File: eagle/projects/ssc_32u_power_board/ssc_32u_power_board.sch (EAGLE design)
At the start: 36 parts, among them J1 691256610002, J10 ESQ-104-24-H-S, J11 ESQ-104-24-H-S, J12 ESQ-104-24-H-S, J13 ESQ-104-24-H-S, J14 MOL-SL-3-RA, J15 ESQ-103-24-H-S, J16 691256610002, J17 HMTSW-104-08-G-S-380, J18 HMTSW-104-08-G-S-380, J19 HMTSW-104-08-G-S-380, J2 HMTSW-104-08-G-S-380, J20 HMTSW-104-08-G-S-380, J21 ESQ-104-24-H-S, J22 ESQ-104-24-H-S, J23 ESQ-104-24-H-S, J24 ESQ-104-24-H-S, J25 ESQ-104-24-H-S, J26 ESQ-104-24-H-S, J27 ESQ-104-24-H-S, J28 ESQ-104-24-H-S, J3 HMTSW-104-08-G-S-380, J4 HMTSW-104-08-G-S-380, J5 HMTSW-104-08-G-S-380, J6 ESQ-104-24-H-S, J7 ESQ-104-24-H-S, J8 ESQ-104-24-H-S, J9 ESQ-104-24-H-S

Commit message: Finished board layout, used polygons to fill all high current traces
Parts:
- removed J10, J11, J12, J13, J21, J22, J23, J24, J25, J26, J27, J28: ESQ-104-24-H-S, ssc_32u_power_board:ESQ-104-24-H-S
- removed J17, J18, J19, J20: HMTSW-104-08-G-S-380, ssc_32u_power_board:HMTSW-104-08-G-S-380
- added F5, F6, F7, F8: 8A, 35V, ssc_32u_power_board:0437008.WR
- F1, F2, F3, F4: value 0751.0507 -> 8A, 35V; device ssc_32u_power_board:0751.0507 -> ssc_32u_power_board:0437008.WR
- J2, J3, J4, J5: value HMTSW-104-08-G-S-380 -> 4x3_2.54MM_HEADER; device ssc_32u_power_board:HMTSW-104-08-G-S-380 -> ssc_32u_power_board:2X_ESQ-104-24-H-S__HMTSW-104-08-G-S-380
- J6, J7, J8, J9: value ESQ-104-24-H-S -> 4x3_2.54MM_HEADER; device ssc_32u_power_board:ESQ-104-24-H-S -> ssc_32u_power_board:2X_ESQ-104-24-H-S__HMTSW-104-08-G-S-380
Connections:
- removed net BATT_1_FUSE_0_7: F1.P$2, S1.P$1
- removed net BATT_1_FUSE_8_15: F2.P$2, S2.P$1
- removed net BATT_1_SWITCH_0_7: J2.P$1, J2.P$2, J2.P$3, J2.P$4, J3.P$1, J3.P$2, J3.P$3, J3.P$4, S1.P$2
- removed net BATT_1_SWITCH_8_15: J4.P$1, J4.P$2, J4.P$3, J4.P$4, J5.P$1, J5.P$2, J5.P$3, J5.P$4, S2.P$2
- removed net BATT_2_FUSE_16_23: F3.P$2, S3.P$1
- removed net BATT_2_FUSE_24_31: F4.P$2, S4.P$1
- removed net BATT_2_SWITCH_16_23: J17.P$1, J17.P$2, J17.P$3, J17.P$4, J18.P$1, J18.P$2, J18.P$3, J18.P$4, S3.P$2
- removed net BATT_2_SWITCH_24_31: J19.P$1, J19.P$2, J19.P$3, J19.P$4, J20.P$1, J20.P$2, J20.P$3, J20.P$4, S4.P$2
- new net VBAT_1_FUSE_0_3: F1.P$2, J2.V1, J2.V2, J2.V3, J2.V4
- new net VBAT_1_FUSE_12_15: F4.P$2, J5.V1, J5.V2, J5.V3, J5.V4
- new net VBAT_1_FUSE_4_7: F2.P$2, J3.V1, J3.V2, J3.V3, J3.V4
- new net VBAT_1_FUSE_8_11: F3.P$2, J4.V1, J4.V2, J4.V3, J4.V4
- new net VBAT_1_SWITCH_0_7: F1.P$1, F2.P$1, S1.P$2
- new net VBAT_1_SWITCH_8_15: F3.P$1, F4.P$1, S2.P$2
- new net VBAT_2_FUSE_16_19: F5.P$2, J6.V1, J6.V2, J6.V3, J6.V4
- new net VBAT_2_FUSE_20_23: F6.P$2, J7.V1, J7.V2, J7.V3, J7.V4
- new net VBAT_2_FUSE_24_27: F7.P$2, J8.V1, J8.V2, J8.V3, J8.V4
- new net VBAT_2_FUSE_28_31: F8.P$2, J9.V1, J9.V2, J9.V3, J9.V4
- new net VBAT_2_SWITCH_16_23: F5.P$1, F6.P$1, S3.P$2
- new net VBAT_2_SWITCH_24_31: F7.P$1, F8.P$1, S4.P$2
- net BATT_1_VDD: now also S1.P$1, S2.P$1; no longer F1.P$1, F2.P$1
- net BATT_2_VDD: now also J16.BAT_VDD, S3.P$1, S4.P$1; no longer F3.P$1, F4.P$1, J16.BAT_GND
- net GND: now also J16.BAT_GND, J2.G1, J2.G2, J2.G3, J2.G4, J3.G1, J3.G2, J3.G3, J3.G4, J4.G1, J4.G2, J4.G3, J4.G4, J5.G1, J5.G2, J5.G3, J5.G4, J6.G1, J6.G2, J6.G3, J6.G4, J7.G1, J7.G2, J7.G3, J7.G4, J8.G1, J8.G2, J8.G3, J8.G4, J9.G1, J9.G2, J9.G3, J9.G4; no longer J10.P$1, J10.P$2, J10.P$3, J10.P$4, J11.P$1, J11.P$2, J11.P$3, J11.P$4, J12.P$1, J12.P$2, J12.P$3, J12.P$4, J13.P$1, J13.P$2, J13.P$3, J13.P$4, J16.BAT_VDD, J25.P$1, J25.P$2, J25.P$3, J25.P$4, J26.P$1, J26.P$2, J26.P$3, J26.P$4, J27.P$1, J27.P$2, J27.P$3, J27.P$4, J28.P$1, J28.P$2, J28.P$3, J28.P$4
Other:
- note removed: "4PPIN GND HEADER - PINS 0-15"
- note removed: "4PPIN GND HEADER - PINS 16-31"
- note removed: "4PPIN PWM HEADER - PINS 0-15"
- note removed: "4PPIN PWM HEADER - PINS 16-31"

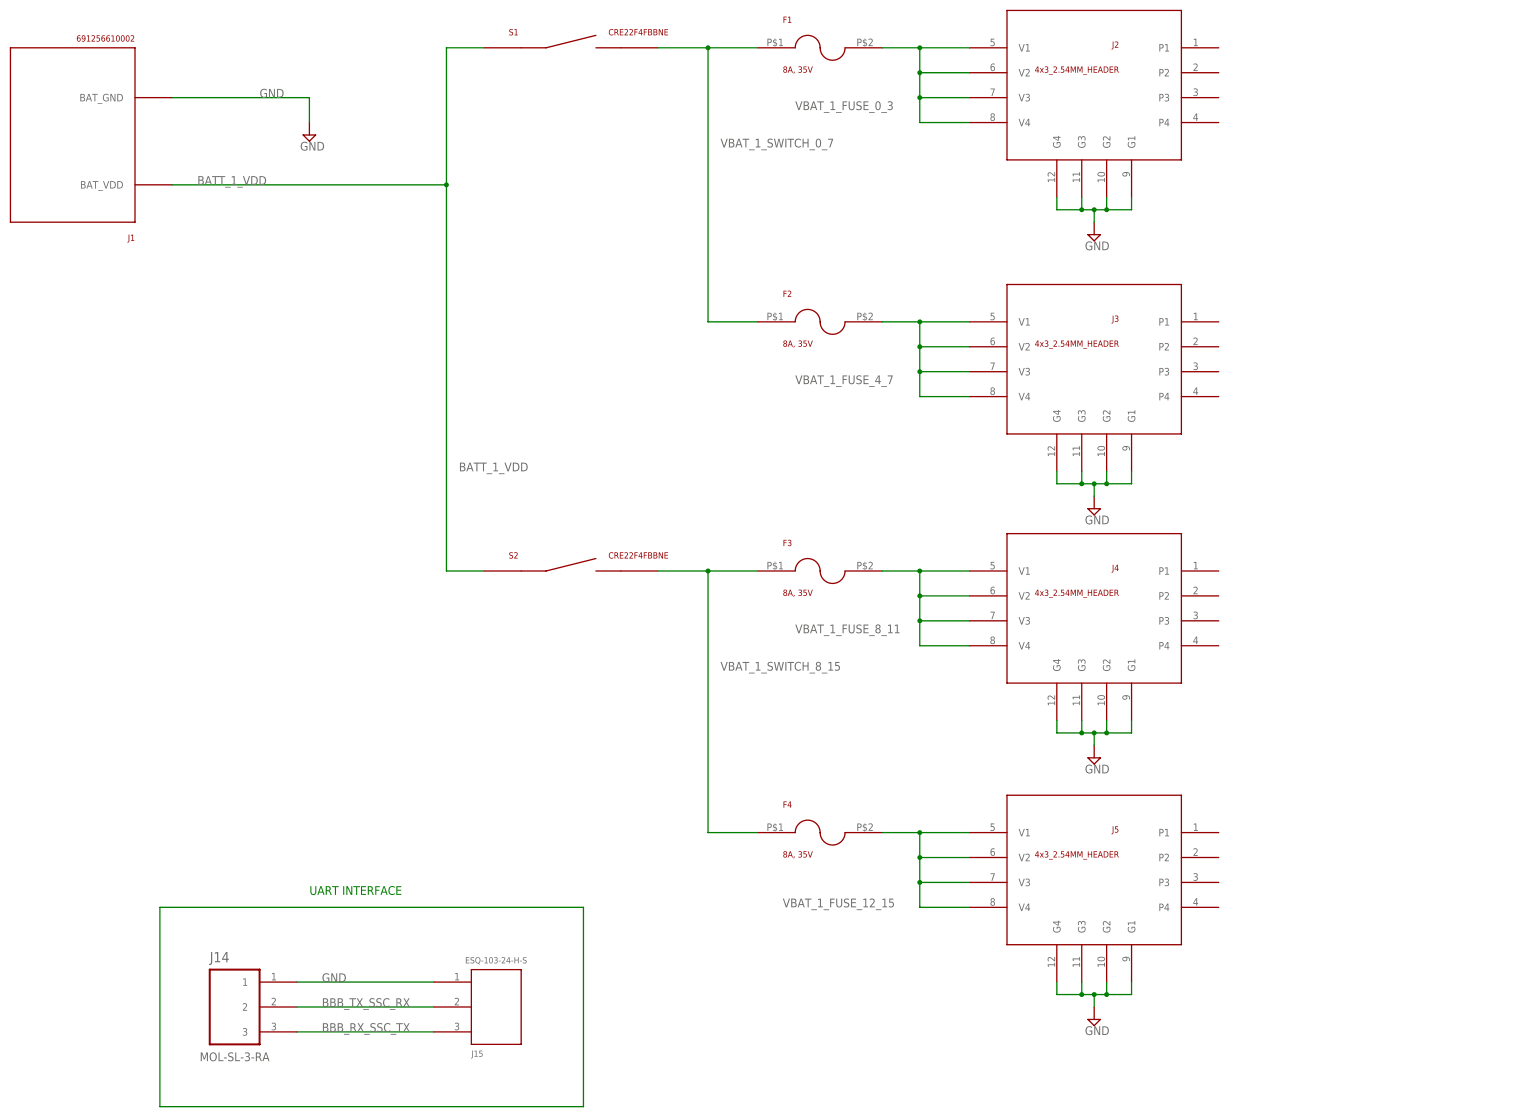
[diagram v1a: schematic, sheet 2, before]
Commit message: Major modifications, removed switches and swapped out surface mount fuses for glass ones. Still two layer board
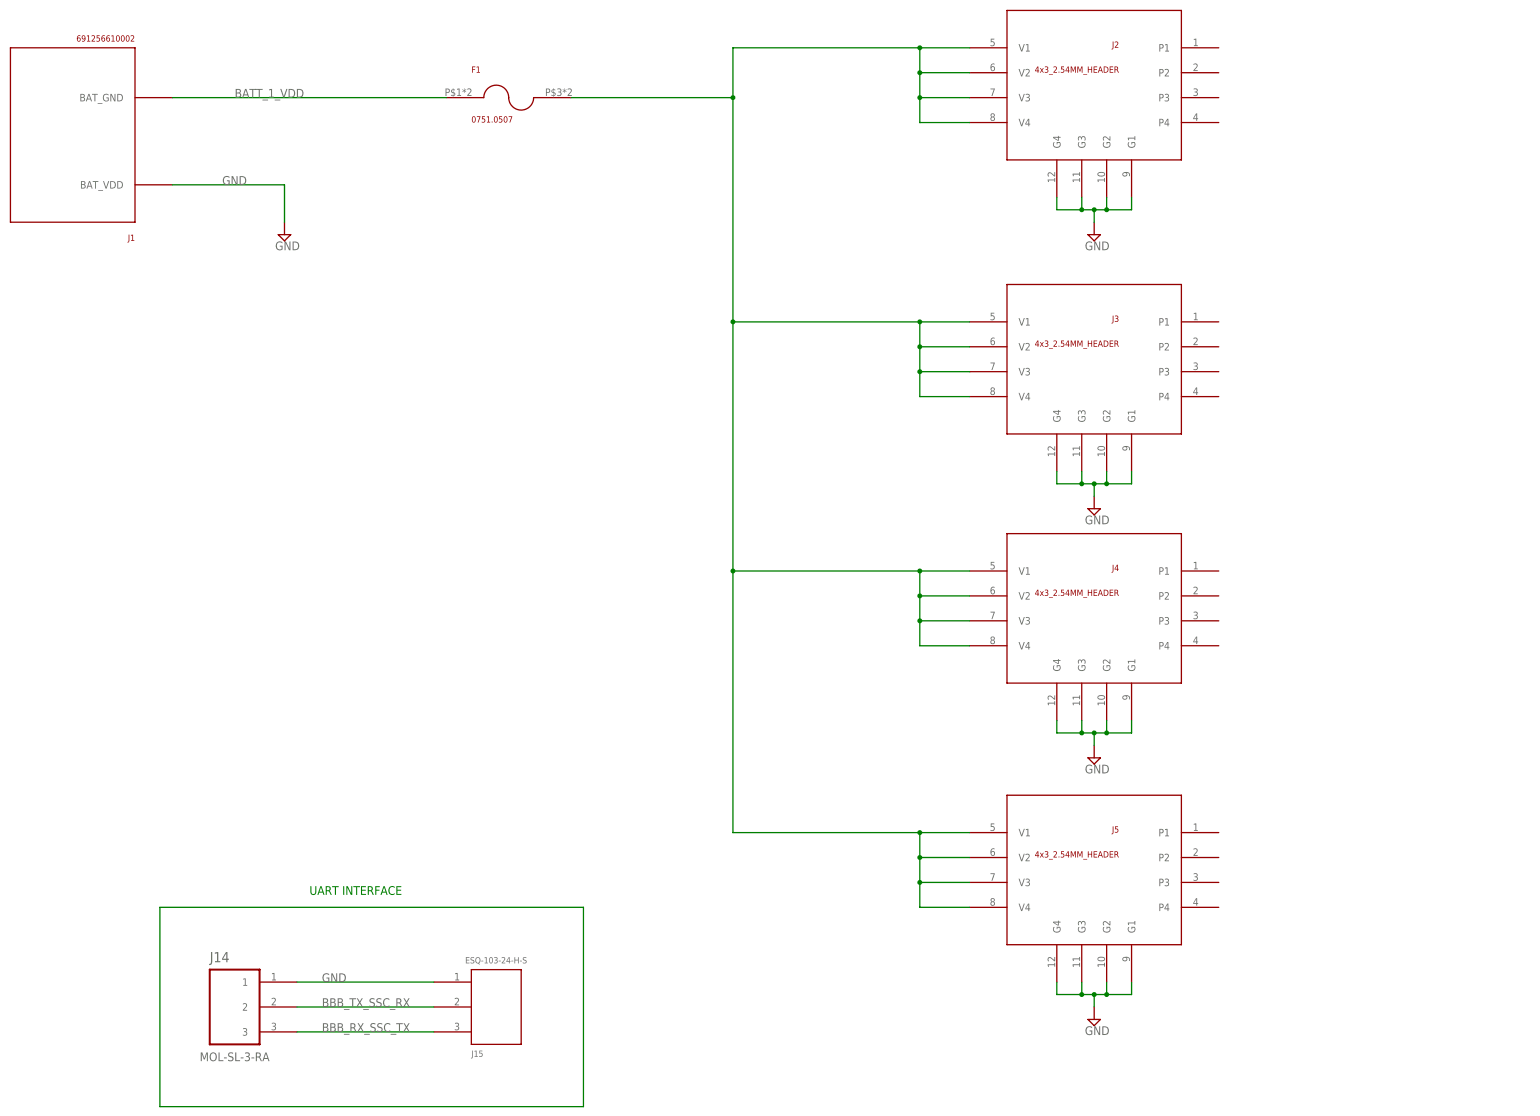
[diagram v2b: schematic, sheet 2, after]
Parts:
- removed F3, F4, F5, F6, F7, F8: 8A, 35V, ssc_32u_power_board:0437008.WR
- removed S1, S2, S3, S4: CRE22F4FBBNE, ssc_32u_power_board:CRE22F4FBBNE
- F1, F2: value 8A, 35V -> 0751.0507; device ssc_32u_power_board:0437008.WR -> ssc_32u_power_board:0751.0507
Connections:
- removed net VBAT_1_FUSE_0_3: F1.P$2, J2.V1, J2.V2, J2.V3, J2.V4
- removed net VBAT_1_FUSE_12_15: F4.P$2, J5.V1, J5.V2, J5.V3, J5.V4
- removed net VBAT_1_FUSE_4_7: F2.P$2, J3.V1, J3.V2, J3.V3, J3.V4
- removed net VBAT_1_FUSE_8_11: F3.P$2, J4.V1, J4.V2, J4.V3, J4.V4
- removed net VBAT_1_SWITCH_0_7: F1.P$1, F2.P$1, S1.P$2
- removed net VBAT_1_SWITCH_8_15: F3.P$1, F4.P$1, S2.P$2
- removed net VBAT_2_FUSE_16_19: F5.P$2, J6.V1, J6.V2, J6.V3, J6.V4
- removed net VBAT_2_FUSE_20_23: F6.P$2, J7.V1, J7.V2, J7.V3, J7.V4
- removed net VBAT_2_FUSE_24_27: F7.P$2, J8.V1, J8.V2, J8.V3, J8.V4
- removed net VBAT_2_FUSE_28_31: F8.P$2, J9.V1, J9.V2, J9.V3, J9.V4
- removed net VBAT_2_SWITCH_16_23: F5.P$1, F6.P$1, S3.P$2
- removed net VBAT_2_SWITCH_24_31: F7.P$1, F8.P$1, S4.P$2
- new net VBAT_1_FUSE_0_15: F1.P$2, J2.V1, J2.V2, J2.V3, J2.V4, J3.V1, J3.V2, J3.V3, J3.V4, J4.V1, J4.V2, J4.V3, J4.V4, J5.V1, J5.V2, J5.V3, J5.V4
- new net VBAT_2_FUSE_16_24_31: F2.P$2, J6.V1, J6.V2, J6.V3, J6.V4, J7.V1, J7.V2, J7.V3, J7.V4, J8.V1, J8.V2, J8.V3, J8.V4, J9.V1, J9.V2, J9.V3, J9.V4
- net BATT_1_VDD: now also F1.P$1, J1.BAT_GND; no longer J1.BAT_VDD, S1.P$1, S2.P$1
- net BATT_2_VDD: now also F2.P$1; no longer S3.P$1, S4.P$1
- net GND: now also J1.BAT_VDD; no longer J1.BAT_GND
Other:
- moved on the sheet: F1

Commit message: Added caps
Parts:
- removed J15: ESQ-103-24-H-S, ssc_32u_power_board:ESQ-103-24-H-S
- added C1, C2: (no value), rcl:CPOL-USE5-13
- added J10: ESQ-104-24-H-S, ssc_32u_power_board:ESQ-104-24-H-S
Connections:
- removed net BBB_RX_SSC_TX: J14.3, J15.P$3
- new net BBB_TX_SSC_TX: J10.P$3, J14.2
- net BBB_TX_SSC_RX: now also J10.P$2, J14.3; no longer J14.2, J15.P$2
- net GND: now also C1.-, C2.-, J10.P$1; no longer J15.P$1
- net VBAT_1_FUSE_0_15: now also C1.+
- net VBAT_2_FUSE_16_24_31: now also C2.+
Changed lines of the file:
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@@
 <part name="SUPPLY1" library="ssc_32u_power_board" deviceset="GND" device=""/>
 <part name="J14" library="ssc_32u_power_board" deviceset="MOLSL_3PIN" device="_RA" technology="_SL3RA" value="MOL-SL-3-RA"/>
-<part name="J15" library="ssc_32u_power_board" deviceset="ESQ-103-24-H-S" device="" value="ESQ-103-24-H-S"/>
 <part name="FRAME3" library="ssc_32u_power_board" deviceset="A3L-LOC" device=""/>
 <part name="J16" library="ssc_32u_power_board" deviceset="691256610002" device="" value="691256610002"/>
@@
 <part name="F1" library="ssc_32u_power_board" deviceset="0751.0507" device="" value="0751.0507"/>
 <part name="F2" library="ssc_32u_power_board" deviceset="0751.0507" device="" value="0751.0507"/>
+<part name="C1" library="rcl" deviceset="CPOL-US" device="E5-13"/>
+<part name="C2" library="rcl" deviceset="CPOL-US" device="E5-13"/>
+<part name="SUPPLY11" library="ssc_32u_power_board" deviceset="GND" device=""/>
+<part name="SUPPLY12" library="ssc_32u_power_board" deviceset="GND" device=""/>
+<part name="J10" library="ssc_32u_power_board" deviceset="ESQ-104-24-H-S" device="" value="ESQ-104-24-H-S"/>
 </parts>
 <sheets>
@@
 <instance part="SUPPLY1" gate="GND" x="96.52" y="198.12"/>
 <instance part="J14" gate="G$1" x="86.36" y="40.64"/>
-<instance part="J15" gate="G$1" x="139.7" y="40.64"/>
 <instance part="SUPPLY2" gate="GND" x="261.62" y="198.12"/>
 <instance part="SUPPLY3" gate="GND" x="261.62" y="142.24"/>
@@
 <instance part="J5" gate="G$1" x="261.62" y="68.58" rot="MR0"/>
 <instance part="F1" gate="G$1" x="142.24" y="226.06"/>
+<instance part="C1" gate="G$1" x="165.1" y="220.98"/>
+<instance part="SUPPLY11" gate="GND" x="165.1" y="210.82"/>
+<instance part="J10" gate="G$1" x="144.78" y="38.1"/>
 </instances>
 <busses>
@@
 <wire x1="73.66" y1="208.28" x2="96.52" y2="208.28" width="0.1524" layer="91"/>
 <label x="83.82" y="208.28" size="1.778" layer="95"/>
-</segment>
-<segment>
-<pinref part="J14" gate="G$1" pin="1"/>
-<pinref part="J15" gate="G$1" pin="P$1"/>
-<wire x1="99.06" y1="45.72" x2="127" y2="45.72" width="0.1524" layer="91"/>
-<label x="104.14" y="45.72" size="1.778" layer="95"/>
 </segment>
 <segment>
@@
 <wire x1="269.24" y1="205.74" x2="269.24" y2="203.2" width="0.1524" layer="91"/>
 </segment>
-</net>
-<net name="BBB_RX_SSC_TX" class="0">
-<segment>
-<pinref part="J14" gate="G$1" pin="3"/>
-<pinref part="J15" gate="G$1" pin="P$3"/>
-<wire x1="99.06" y1="35.56" x2="127" y2="35.56" width="0.1524" layer="91"/>
-<label x="104.14" y="35.56" size="1.778" layer="95"/>
+<segment>
+<pinref part="C1" gate="G$1" pin="-"/>
+<pinref part="SUPPLY11" gate="GND" pin="GND"/>
+<wire x1="165.1" y1="215.9" x2="165.1" y2="213.36" width="0.1524" layer="91"/>
+</segment>
+<segment>
+<pinref part="J14" gate="G$1" pin="1"/>
+<wire x1="99.06" y1="45.72" x2="132.08" y2="45.72" width="0.1524" layer="91"/>
+<label x="104.14" y="45.72" size="1.778" layer="95"/>
+<pinref part="J10" gate="G$1" pin="P$1"/>
 </segment>
 </net>
@@
 <wire x1="157.48" y1="20.32" x2="71.12" y2="20.32" width="0.1524" layer="91"/>
 <wire x1="71.12" y1="20.32" x2="71.12" y2="60.96" width="0.1524" layer="91"/>
-</segment>
-</net>
-<net name="BBB_TX_SSC_RX" class="0">
-<segment>
-<pinref part="J14" gate="G$1" pin="2"/>
-<pinref part="J15" gate="G$1" pin="P$2"/>
-<wire x1="99.06" y1="40.64" x2="127" y2="40.64" width="0.1524" layer="91"/>
-<label x="104.14" y="40.64" size="1.778" layer="95"/>
 </segment>
 </net>
@@
 <wire x1="187.96" y1="236.22" x2="226.06" y2="236.22" width="0.1524" layer="91"/>
 <pinref part="F1" gate="G$1" pin="P$2"/>
-<wire x1="154.94" y1="226.06" x2="187.96" y2="226.06" width="0.1524" layer="91"/>
+<wire x1="154.94" y1="226.06" x2="165.1" y2="226.06" width="0.1524" layer="91"/>
+<wire x1="165.1" y1="226.06" x2="187.96" y2="226.06" width="0.1524" layer="91"/>
 <wire x1="187.96" y1="226.06" x2="187.96" y2="236.22" width="0.1524" layer="91"/>
 <wire x1="226.06" y1="60.96" x2="226.06" y2="66.04" width="0.1524" layer="91"/>
@@
 <wire x1="226.06" y1="180.34" x2="187.96" y2="180.34" width="0.1524" layer="91"/>
 <junction x="187.96" y="180.34"/>
+<pinref part="C1" gate="G$1" pin="+"/>
+<wire x1="165.1" y1="226.06" x2="165.1" y2="223.52" width="0.1524" layer="91"/>
+<junction x="165.1" y="226.06"/>
 </segment>
 </net>
@@
 <pinref part="F1" gate="G$1" pin="P$1"/>
 <label x="86.36" y="226.06" size="1.778" layer="95"/>
+</segment>
+</net>
+<net name="BBB_TX_SSC_RX" class="0">
+<segment>
+<pinref part="J14" gate="G$1" pin="3"/>
+<wire x1="99.06" y1="35.56" x2="114.3" y2="35.56" width="0.1524" layer="91"/>
+<wire x1="114.3" y1="35.56" x2="114.3" y2="40.64" width="0.1524" layer="91"/>
+<pinref part="J10" gate="G$1" pin="P$2"/>
+<wire x1="114.3" y1="40.64" x2="132.08" y2="40.64" width="0.1524" layer="91"/>
+</segment>
+</net>
+<net name="BBB_TX_SSC_TX" class="0">
+<segment>
+<pinref part="J14" gate="G$1" pin="2"/>
+<wire x1="99.06" y1="40.64" x2="109.22" y2="40.64" width="0.1524" layer="91"/>
+<wire x1="109.22" y1="40.64" x2="109.22" y2="38.1" width="0.1524" layer="91"/>
+<wire x1="109.22" y1="38.1" x2="119.38" y2="38.1" width="0.1524" layer="91"/>
+<wire x1="119.38" y1="38.1" x2="119.38" y2="35.56" width="0.1524" layer="91"/>
+<pinref part="J10" gate="G$1" pin="P$3"/>
+<wire x1="119.38" y1="35.56" x2="132.08" y2="35.56" width="0.1524" layer="91"/>
 </segment>
 </net>
@@
 <instance part="SUPPLY6" gate="GND" x="96.52" y="175.26"/>
 <instance part="F2" gate="G$1" x="147.32" y="200.66"/>
+<instance part="C2" gate="G$1" x="167.64" y="190.5"/>
+<instance part="SUPPLY12" gate="GND" x="167.64" y="180.34"/>
 </instances>
 <busses>
@@
 <wire x1="96.52" y1="182.88" x2="96.52" y2="177.8" width="0.1524" layer="91"/>
 </segment>
+<segment>
+<pinref part="C2" gate="G$1" pin="-"/>
+<pinref part="SUPPLY12" gate="GND" pin="GND"/>
+<wire x1="167.64" y1="185.42" x2="167.64" y2="182.88" width="0.1524" layer="91"/>
+</segment>
 </net>
 <net name="BATT_2_VDD" class="0">
@@
 <wire x1="200.66" y1="238.76" x2="256.54" y2="238.76" width="0.1524" layer="91"/>
 <pinref part="F2" gate="G$1" pin="P$2"/>
-<wire x1="160.02" y1="200.66" x2="200.66" y2="200.66" width="0.1524" layer="91"/>
+<wire x1="160.02" y1="200.66" x2="167.64" y2="200.66" width="0.1524" layer="91"/>
+<wire x1="167.64" y1="200.66" x2="200.66" y2="200.66" width="0.1524" layer="91"/>
 <wire x1="200.66" y1="200.66" x2="200.66" y2="238.76" width="0.1524" layer="91"/>
 <wire x1="256.54" y1="55.88" x2="256.54" y2="60.96" width="0.1524" layer="91"/>
@@
 <label x="228.6" y="167.64" size="1.778" layer="95"/>
 <junction x="200.66" y="182.88"/>
-</segment>
-</net>
+<pinref part="C2" gate="G$1" pin="+"/>
+<wire x1="167.64" y1="193.04" x2="167.64" y2="200.66" width="0.1524" layer="91"/>
+<junction x="167.64" y="200.66"/>
+</segment>
+</net>
